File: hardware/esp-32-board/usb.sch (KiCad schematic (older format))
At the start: 14 parts, among them J7 USB_B_Micro, Q1 BCR129S, U4 USBLC6-2SC6, U5 FT232RL

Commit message: Remove serial resistors for USB (FT232RL has own serial resistors).
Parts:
- removed R2, R3: 22 Ohm, Resistor_SMD:R_0805_2012Metric_Pad1.20x1.40mm_HandSolder, symbol Device:R
- renumbered R4 to R2, R5 to R3, R6 to R4
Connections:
- net USB_DN: now also U4.3 (I/O2)
- net USB_DP: now also U4.1 (I/O1)
- net at J7.2 (D-): now also U4.4 (I/O2); no longer U4.6 (I/O1)
- net at J7.3 (D+): now also U4.6 (I/O1); no longer U4.4 (I/O2)
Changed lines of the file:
@@
 P 5050 3300
 AR Path="/5FFBA107" Ref="R?"  Part="1"
-AR Path="/5FF73D59/5FFBA107" Ref="R4"  Part="1"
-F 0 "R4" V 5150 3350 50  0000 R CNN
+AR Path="/5FF73D59/5FFBA107" Ref="R2"  Part="1"
+F 0 "R2" V 5150 3350 50  0000 R CNN
 F 1 "2.2k Ohm" V 5250 3450 50  0000 R CNN
 F 2 "Resistor_SMD:R_0805_2012Metric_Pad1.20x1.40mm_HandSolder" V 4980 3300 50  0001 C CNN
@@
 	9350 3700 9600 3700
 $Comp
-L Device:R R5
+L Device:R R3
 U 1 1 5FFD83B8
 P 9100 4350
-F 0 "R5" H 9200 4400 50  0000 L CNN
+F 0 "R3" H 9200 4400 50  0000 L CNN
 F 1 "220 Ohm" H 9200 4350 50  0000 L CNN
 F 2 "Resistor_SMD:R_0805_2012Metric_Pad1.20x1.40mm_HandSolder" V 9030 4350 50  0001 C CNN
@@
 $EndComp
 $Comp
-L Device:R R6
+L Device:R R4
 U 1 1 5FFDD2E6
 P 9600 4350
-F 0 "R6" H 9700 4400 50  0000 L CNN
+F 0 "R4" H 9700 4400 50  0000 L CNN
 F 1 "220 Ohm" H 9700 4350 50  0000 L CNN
 F 2 "Resistor_SMD:R_0805_2012Metric_Pad1.20x1.40mm_HandSolder" V 9530 4350 50  0001 C CNN
@@
 F 5 "https://www.tme.eu/pl/details/usblc6-2sc6/diody-zabezpieczajace-drabinki/stmicroelectronics/" H 2700 2800 50  0001 C CNN "VendorLink"
 	1    2700 2800
-	0    -1   -1   0
-$EndComp
-Wire Wire Line
-	2800 2350 2900 2350
-Wire Wire Line
-	3200 2350 3350 2350
-Wire Wire Line
-	2800 3250 2900 3250
-Wire Wire Line
-	3200 3250 3350 3250
-$Comp
-L Device:R R?
-U 1 1 5FC43B6A
-P 3050 3250
-AR Path="/5FC43B6A" Ref="R?"  Part="1"
-AR Path="/5FF73D59/5FC43B6A" Ref="R3"  Part="1"
-F 0 "R3" V 2950 3400 50  0000 R CNN
-F 1 "22 Ohm" V 2950 3250 50  0000 R CNN
-F 2 "Resistor_SMD:R_0805_2012Metric_Pad1.20x1.40mm_HandSolder" V 2980 3250 50  0001 C CNN
-F 3 "~" H 3050 3250 50  0001 C CNN
-F 4 "avt.pl" H 3050 3250 50  0001 C CNN "Vendor"
-F 5 "https://sklep.avt.pl/avt701-805.html" H 3050 3250 50  0001 C CNN "VendorLink"
-	1    3050 3250
-	0    -1   -1   0
-$EndComp
-$Comp
-L Device:R R?
-U 1 1 5FC3959C
-P 3050 2350
-AR Path="/5FC3959C" Ref="R?"  Part="1"
-AR Path="/5FF73D59/5FC3959C" Ref="R2"  Part="1"
-F 0 "R2" V 3150 2500 50  0000 R CNN
-F 1 "22 Ohm" V 3150 2350 50  0000 R CNN
-F 2 "Resistor_SMD:R_0805_2012Metric_Pad1.20x1.40mm_HandSolder" V 2980 2350 50  0001 C CNN
-F 3 "~" H 3050 2350 50  0001 C CNN
-F 4 "avt.pl" H 3050 2350 50  0001 C CNN "Vendor"
-F 5 "https://sklep.avt.pl/avt701-805.html" H 3050 2350 50  0001 C CNN "VendorLink"
-	1    3050 2350
-	0    -1   -1   0
-$EndComp
+	0    -1   1    0
+$EndComp
+Wire Wire Line
+	2800 2350 3350 2350
+Wire Wire Line
+	2800 3250 3350 3250
 $EndSCHEMATC

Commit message: Fix RX/TX led polarity
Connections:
- net USB_3V3: now also D4.2 (A), D5.2 (A); no longer D4.1 (K), D5.1 (K)
- net at R3.1: now also D4.1 (K); no longer D4.2 (A)
- net at R4.1: now also D5.1 (K); no longer D5.2 (A)
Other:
- moved on the sheet: D4, D5
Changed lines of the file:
@@
 F 5 "https://www.tme.eu/pl/details/rf-yus150ts-ae/diody-led-smd-kolorowe/refond/" H 9100 3950 50  0001 C CNN "VendorLink"
 	1    9100 3950
-	0    1    1    0
+	0    1    -1   0
 $EndComp
 $Comp
@@
 F 5 "https://www.tme.eu/pl/details/rf-yus150ts-ae/diody-led-smd-kolorowe/refond/" H 9600 3950 50  0001 C CNN "VendorLink"
 	1    9600 3950
-	0    1    1    0
+	0    1    -1   0
 $EndComp
 Text Label 9000 4650 2    50   ~ 0

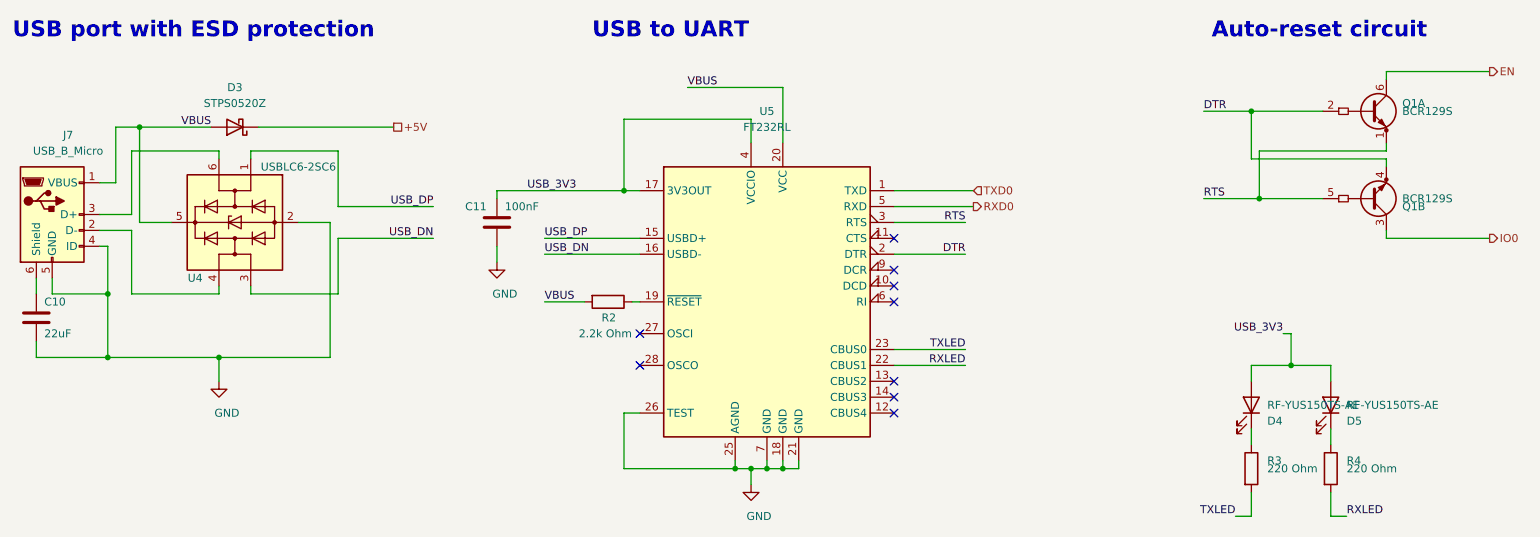
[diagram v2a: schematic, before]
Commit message: Replace Micro USB and button components (no products in stock)
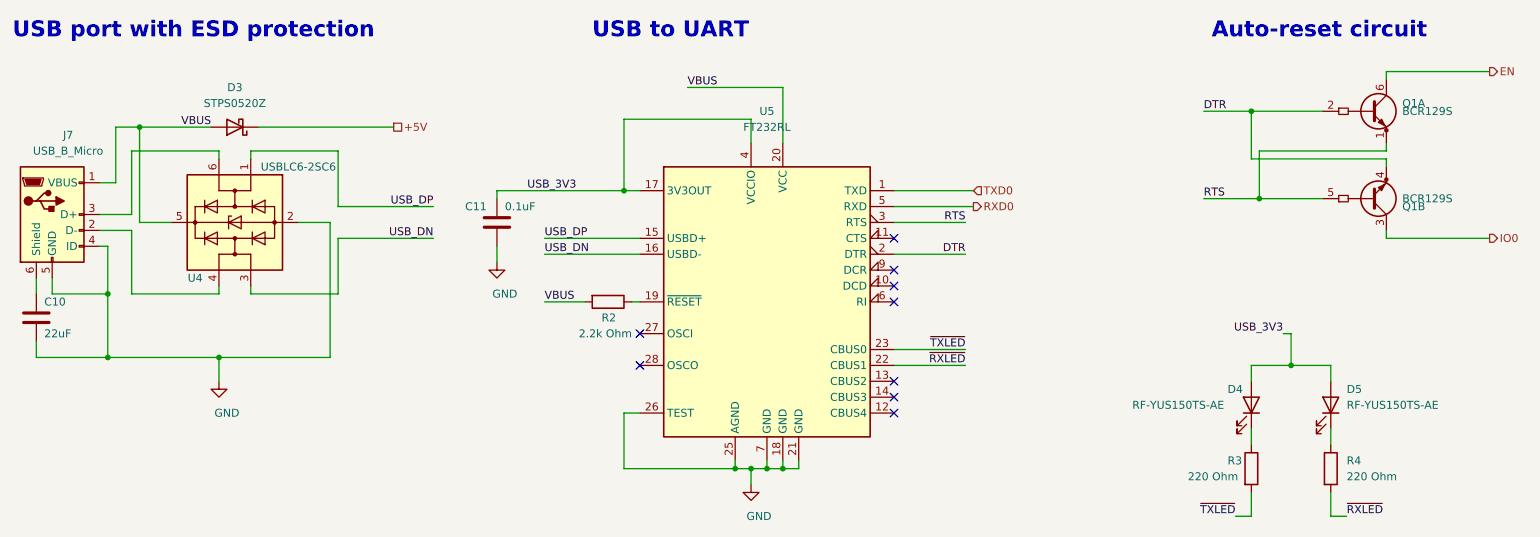
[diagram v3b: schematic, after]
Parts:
- C11: value 100nF -> 0.1uF
- J7: footprint Connector_USB:USB_Micro-B_Molex-105017-0001 -> Connector_USB:USB_Micro-B_Amphenol_10118194_Horizontal; VendorLink https://www.tme.eu/pl/details/mx-105017-0001/zlacza-usb-i-i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 -> https://www.tme.eu/pl/details/10118194-0001lf_c/zlacza-usb-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
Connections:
- net RXLED renamed ~RXLED
- net TXLED renamed ~TXLED
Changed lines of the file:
@@
 F 0 "J7" H 1650 3250 50  0000 C CNN
 F 1 "USB_B_Micro" H 1650 3150 50  0000 C CNN
-F 2 "Connector_USB:USB_Micro-B_Molex-105017-0001" H 1700 2700 50  0001 C CNN
-F 3 "https://www.tme.eu/Document/b7989e722b05f5084c507fb3ad8f02cb/MX-105017-0001.pdf" H 1700 2700 50  0001 C CNN
+F 2 "Connector_USB:USB_Micro-B_Amphenol_10118194_Horizontal" H 1700 2700 50  0001 C CNN
+F 3 "https://www.tme.eu/Document/224991b12752feb77f9b8261a1cec430/10118194-0001LF.pdf" H 1700 2700 50  0001 C CNN
 F 4 "tme.eu" H 1550 2750 50  0001 C CNN "Vendor"
-F 5 "https://www.tme.eu/pl/details/mx-105017-0001/zlacza-usb-i-ieee1394/molex/105017-0001/" H 1550 2750 50  0001 C CNN "VendorLink"
+F 5 "https://www.tme.eu/pl/details/10118194-0001lf_c/zlacza-usb-i-ieee1394/amphenol/10118194-0001lf/" H 1550 2750 50  0001 C CNN "VendorLink"
 	1    1550 2750
 	1    0    0    -1
@@
 P 4350 2800
 F 0 "C11" H 4150 2900 50  0000 L CNN
-F 1 "100nF" H 4400 2900 50  0000 L CNN
+F 1 "0.1uF" H 4400 2900 50  0000 L CNN
 F 2 "Capacitor_SMD:C_0805_2012Metric_Pad1.18x1.45mm_HandSolder" H 4388 2650 50  0001 C CNN
 F 3 "~" H 4350 2800 50  0001 C CNN
@@
 NoConn ~ 5250 3700
 Text Label 7300 3700 2    50   ~ 0
-RXLED
+~RXLED
 Text Label 7300 3600 2    50   ~ 0
-TXLED
+~TXLED
 Wire Wire Line
 	6850 3600 7300 3600
@@
 U 1 1 5FFCB60F
 P 9100 3950
-F 0 "D4" V 9000 4050 50  0000 L CNN
-F 1 "RF-YUS150TS-AE" V 9100 4050 50  0000 L CNN
+F 0 "D4" V 9200 3800 50  0000 L CNN
+F 1 "RF-YUS150TS-AE" V 9100 3200 50  0000 L CNN
 F 2 "LED_SMD:LED_1206_3216Metric_Pad1.42x1.75mm_HandSolder" H 9100 3950 50  0001 C CNN
 F 3 "https://www.tme.eu/Document/4237cf95222820e492ff101ceed40a8c/RF-YUS150TS-AE.pdf" H 9100 3950 50  0001 C CNN
@@
 U 1 1 5FFCC087
 P 9600 3950
-F 0 "D5" V 9500 4050 50  0000 L CNN
+F 0 "D5" V 9700 4050 50  0000 L CNN
 F 1 "RF-YUS150TS-AE" V 9600 4050 50  0000 L CNN
 F 2 "LED_SMD:LED_1206_3216Metric_Pad1.42x1.75mm_HandSolder" H 9600 3950 50  0001 C CNN
@@
 $EndComp
 Text Label 9000 4650 2    50   ~ 0
-TXLED
+~TXLED
 Wire Wire Line
 	9000 4650 9100 4650
@@
 	9100 4650 9100 4500
 Text Label 9700 4650 0    50   ~ 0
-RXLED
+~RXLED
 Wire Wire Line
 	9600 4500 9600 4650
@@
 U 1 1 5FFD83B8
 P 9100 4350
-F 0 "R3" H 9200 4400 50  0000 L CNN
-F 1 "220 Ohm" H 9200 4350 50  0000 L CNN
+F 0 "R3" H 8950 4400 50  0000 L CNN
+F 1 "220 Ohm" H 8700 4300 50  0000 L CNN
 F 2 "Resistor_SMD:R_0805_2012Metric_Pad1.20x1.40mm_HandSolder" V 9030 4350 50  0001 C CNN
 F 3 "~" H 9100 4350 50  0001 C CNN
@@
 P 9600 4350
 F 0 "R4" H 9700 4400 50  0000 L CNN
-F 1 "220 Ohm" H 9700 4350 50  0000 L CNN
+F 1 "220 Ohm" H 9700 4300 50  0000 L CNN
 F 2 "Resistor_SMD:R_0805_2012Metric_Pad1.20x1.40mm_HandSolder" V 9530 4350 50  0001 C CNN
 F 3 "~" H 9600 4350 50  0001 C CNN

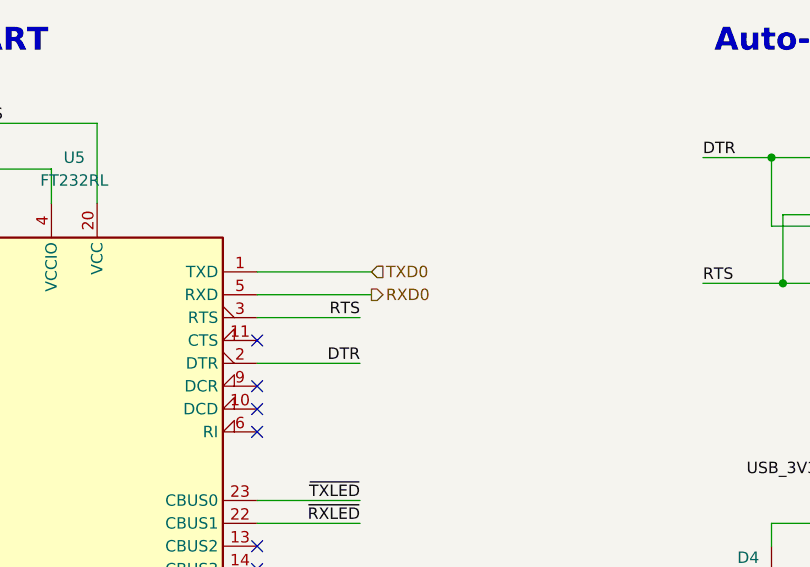
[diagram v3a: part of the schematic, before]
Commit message: Swap RX and TX on FT232RL
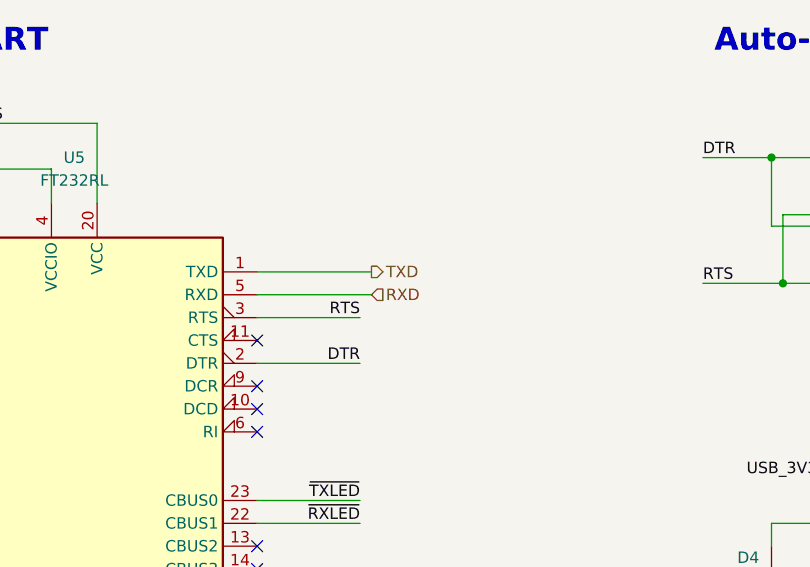
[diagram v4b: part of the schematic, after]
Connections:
- net RXD0 renamed RXD
- net TXD0 renamed TXD
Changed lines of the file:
@@
 Text HLabel 10600 2900 2    50   Output ~ 0
 IO0
-Text HLabel 7350 2600 2    50   Input ~ 0
-TXD0
-Text HLabel 7350 2700 2    50   Output ~ 0
-RXD0
 Text Label 7300 3000 2    50   ~ 0
 DTR
@@
 	6850 2800 7300 2800
 Wire Wire Line
-	6850 2600 7350 2600
-Wire Wire Line
-	6850 2700 7350 2700
-Wire Wire Line
 	5850 4300 5850 4350
 Wire Wire Line
@@
 Wire Wire Line
 	2800 3250 3350 3250
+Wire Wire Line
+	6850 2700 7350 2700
+Text HLabel 7350 2700 2    50   Input ~ 0
+RXD
+Wire Wire Line
+	6850 2600 7350 2600
+Text HLabel 7350 2600 2    50   Output ~ 0
+TXD
 $EndSCHEMATC

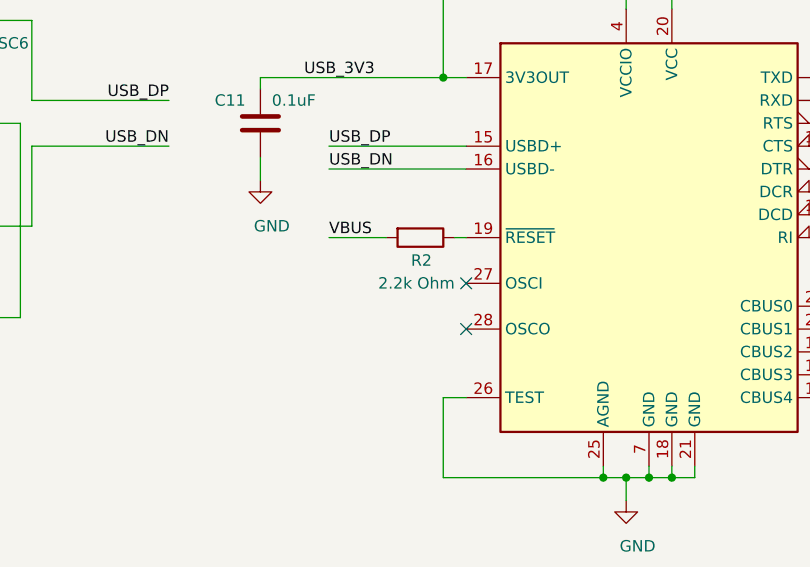
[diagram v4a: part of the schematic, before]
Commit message: CI: fix errors (#2)
* CI: fix errors

* Cosmetic fixes on PCB

* Change build trigger conditions

* Regenerate cooper zones

* Cosmetic fixes on PCB

* Mark ESP-PROG as SMD
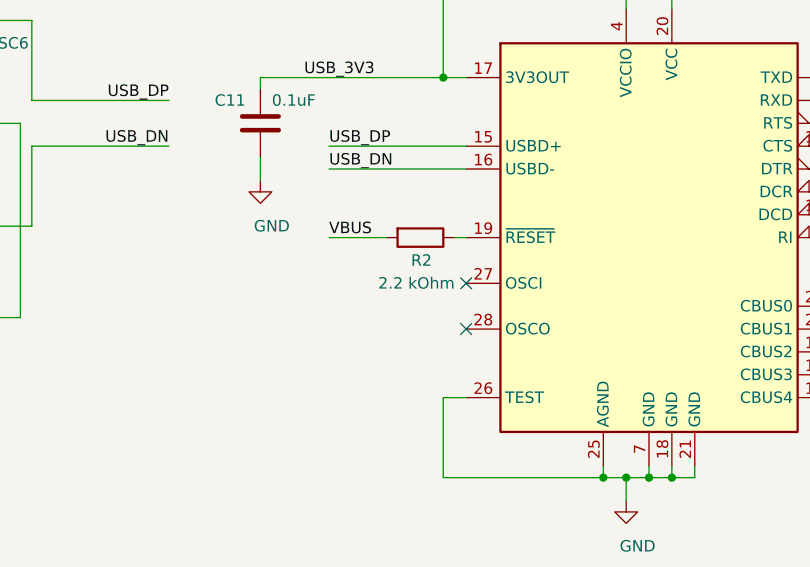
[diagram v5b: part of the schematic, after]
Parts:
- R2: value 2.2k Ohm -> 2.2 kOhm
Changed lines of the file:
@@
 AR Path="/5FF73D59/5FFBA107" Ref="R2"  Part="1"
 F 0 "R2" V 5150 3350 50  0000 R CNN
-F 1 "2.2k Ohm" V 5250 3450 50  0000 R CNN
+F 1 "2.2 kOhm" V 5250 3450 50  0000 R CNN
 F 2 "Resistor_SMD:R_0805_2012Metric_Pad1.20x1.40mm_HandSolder" V 4980 3300 50  0001 C CNN
 F 3 "~" H 5050 3300 50  0001 C CNN
